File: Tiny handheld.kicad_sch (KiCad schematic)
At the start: 38 parts, among them J1 Conn_01x04_Female, J2 Conn_01x04_Female, J3 TYPE-C-31-M-12, U1 ATtiny85-20P, U2 ATtiny85-20M, U3 EEPROM-I2CEIAJ

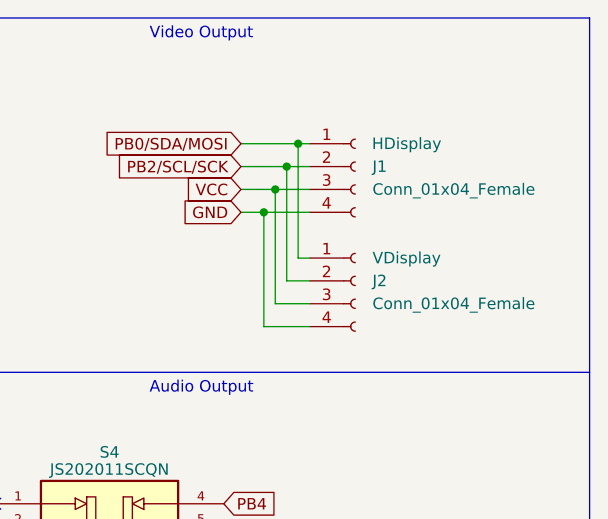
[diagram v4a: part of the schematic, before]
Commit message: removed vertical screen header
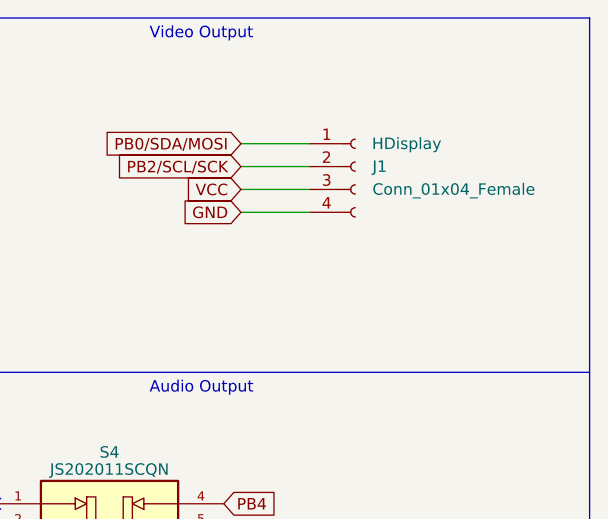
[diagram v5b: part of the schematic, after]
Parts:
- removed J2: Conn_01x04_Female, Connector_PinHeader_2.54mm:PinHeader_1x04_P2.54mm_Vertical, symbol Connector:Conn_01x04_Female
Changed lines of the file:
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@@
   (junction (at 132.715 57.15) (diameter 0) (color 0 0 0 0)
   )
-  (junction (at 245.745 34.925) (diameter 0) (color 0 0 0 0)
-  )
   (junction (at 130.175 29.845) (diameter 0) (color 0 0 0 0)
   )
@@
   (junction (at 54.61 100.33) (diameter 0) (color 0 0 0 0)
   )
-  (junction (at 249.555 27.305) (diameter 0) (color 0 0 0 0)
-  )
-  (junction (at 248.285 29.845) (diameter 0) (color 0 0 0 0)
-  )
   (junction (at 132.715 54.61) (diameter 0) (color 0 0 0 0)
   )
@@
   )
   (junction (at 36.83 34.925) (diameter 0) (color 0 0 0 0)
-  )
-  (junction (at 247.015 32.385) (diameter 0) (color 0 0 0 0)
   )
   (junction (at 130.175 32.385) (diameter 0) (color 0 0 0 0)
@@
     (stroke (width 0) (type default) (color 0 0 0 0))
   )
-  (wire (pts (xy 247.015 45.085) (xy 247.015 32.385))
-    (stroke (width 0) (type default) (color 0 0 0 0))
-  )
   (wire (pts (xy 123.825 107.315) (xy 128.905 107.315))
     (stroke (width 0) (type default) (color 0 0 0 0))
@@
     (stroke (width 0) (type default) (color 0 0 0 0))
   )
-  (wire (pts (xy 250.825 45.085) (xy 247.015 45.085))
-    (stroke (width 0) (type default) (color 0 0 0 0))
-  )
   (wire (pts (xy 35.56 70.485) (xy 39.37 70.485))
     (stroke (width 0) (type default) (color 0 0 0 0))
@@
     (stroke (width 0) (type default) (color 0 0 0 0))
   )
-  (wire (pts (xy 250.825 42.545) (xy 248.285 42.545))
-    (stroke (width 0) (type default) (color 0 0 0 0))
-  )
-  (wire (pts (xy 243.205 32.385) (xy 247.015 32.385))
-    (stroke (width 0) (type default) (color 0 0 0 0))
-  )
   (wire (pts (xy 53.34 57.785) (xy 53.34 61.595))
     (stroke (width 0) (type default) (color 0 0 0 0))
@@
     (stroke (width 0) (type default) (color 0 0 0 0))
   )
-  (wire (pts (xy 248.285 29.845) (xy 250.825 29.845))
+  (wire (pts (xy 243.205 29.845) (xy 250.825 29.845))
     (stroke (width 0) (type default) (color 0 0 0 0))
   )
@@
     (stroke (width 0) (type default) (color 0 0 0 0))
   )
-  (wire (pts (xy 245.745 34.925) (xy 250.825 34.925))
-    (stroke (width 0) (type default) (color 0 0 0 0))
-  )
-  (wire (pts (xy 250.825 47.625) (xy 245.745 47.625))
+  (wire (pts (xy 243.205 34.925) (xy 250.825 34.925))
     (stroke (width 0) (type default) (color 0 0 0 0))
   )
@@
     (stroke (width 0) (type default) (color 0 0 0 0))
   )
-  (wire (pts (xy 250.825 40.005) (xy 249.555 40.005))
-    (stroke (width 0) (type default) (color 0 0 0 0))
-  )
   (wire (pts (xy 53.34 83.185) (xy 53.34 85.725))
     (stroke (width 0) (type default) (color 0 0 0 0))
@@
     (stroke (width 0) (type default) (color 0 0 0 0))
   )
-  (wire (pts (xy 243.205 34.925) (xy 245.745 34.925))
-    (stroke (width 0) (type default) (color 0 0 0 0))
-  )
   (wire (pts (xy 167.005 32.385) (xy 173.355 32.385))
     (stroke (width 0) (type default) (color 0 0 0 0))
@@
     (stroke (width 0) (type default) (color 0 0 0 0))
   )
-  (wire (pts (xy 248.285 42.545) (xy 248.285 29.845))
-    (stroke (width 0) (type default) (color 0 0 0 0))
-  )
-  (wire (pts (xy 245.745 47.625) (xy 245.745 34.925))
-    (stroke (width 0) (type default) (color 0 0 0 0))
-  )
   (wire (pts (xy 42.545 111.76) (xy 42.545 114.3))
     (stroke (width 0) (type default) (color 0 0 0 0))
@@
     (stroke (width 0) (type default) (color 0 0 0 0))
   )
-  (wire (pts (xy 243.205 27.305) (xy 249.555 27.305))
+  (wire (pts (xy 243.205 27.305) (xy 250.825 27.305))
     (stroke (width 0) (type default) (color 0 0 0 0))
   )
@@
     (stroke (width 0) (type default) (color 0 0 0 0))
   )
-  (wire (pts (xy 249.555 40.005) (xy 249.555 27.305))
-    (stroke (width 0) (type default) (color 0 0 0 0))
-  )
-  (wire (pts (xy 247.015 32.385) (xy 250.825 32.385))
+  (wire (pts (xy 243.205 32.385) (xy 250.825 32.385))
     (stroke (width 0) (type default) (color 0 0 0 0))
   )
@@
     (stroke (width 0) (type default) (color 0 0 0 0))
   )
-  (wire (pts (xy 249.555 27.305) (xy 250.825 27.305))
-    (stroke (width 0) (type default) (color 0 0 0 0))
-  )
   (wire (pts (xy 42.545 116.84) (xy 42.545 119.38))
     (stroke (width 0) (type default) (color 0 0 0 0))
   )
   (wire (pts (xy 45.72 119.38) (xy 56.515 119.38))
-    (stroke (width 0) (type default) (color 0 0 0 0))
-  )
-  (wire (pts (xy 243.205 29.845) (xy 248.285 29.845))
     (stroke (width 0) (type default) (color 0 0 0 0))
   )
@@
     (pin "2")
   )
-  (symbol (lib_id "Connector:Conn_01x04_Female") (at 255.905 42.545 0) (unit 1)
-    (in_bom yes) (on_board yes)
-    (property "Reference" "J2" (id 0) (at 257.81 42.5449 0)
-      (effects (font (size 1.27 1.27)) (justify left))
-    )
-    (property "Value" "Conn_01x04_Female" (id 1) (at 257.81 45.0849 0)
-      (effects (font (size 1.27 1.27)) (justify left))
-    )
-    (property "Footprint" "Connector_PinHeader_2.54mm:PinHeader_1x04_P2.54mm_Vertical" (id 2) (at 255.905 42.545 0)
-      (effects (font (size 1.27 1.27)) hide)
-    )
-    (property "Datasheet" "~" (id 3) (at 255.905 42.545 0)
-      (effects (font (size 1.27 1.27)) hide)
-    )
-    (property "Purpose" "VDisplay" (id 4) (at 261.62 40.005 0))
-    (pin "1")
-    (pin "2")
-    (pin "3")
-    (pin "4")
-  )
   (symbol (lib_id "power:GND") (at 250.19 81.915 0) (unit 1)
     (in_bom yes) (on_board yes) (fields_autoplaced)
@@
       (reference "J1") (unit 1) (value "Conn_01x04_Female") (footprint "Connector_PinHeader_2.54mm:PinHeader_1x04_P2.54mm_Vertical")
     )
-    (path "/9e146ef5-55d1-47a4-b06d-46cb8cec31e9"
-      (reference "J2") (unit 1) (value "Conn_01x04_Female") (footprint "Connector_PinHeader_2.54mm:PinHeader_1x04_P2.54mm_Vertical")
-    )
     (path "/3f447363-eab1-44cf-bd61-e64a97ca5167"

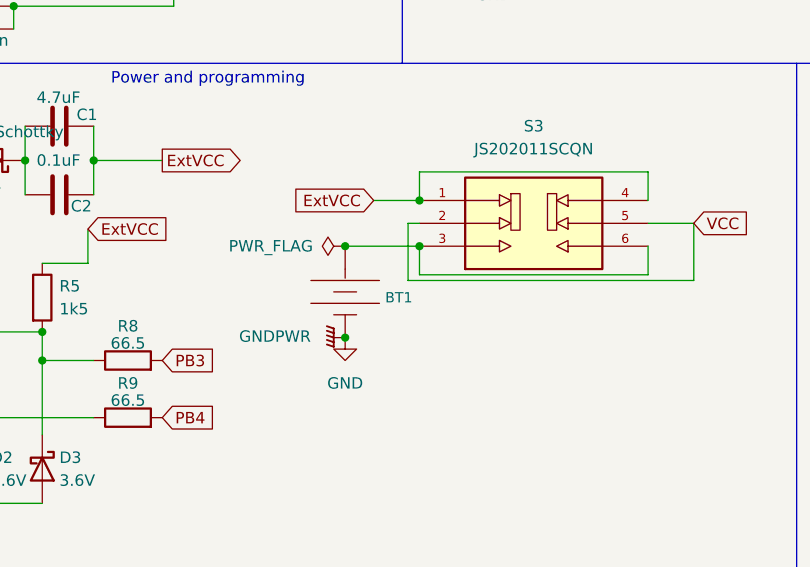
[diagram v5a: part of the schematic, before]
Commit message: first melted circuit tryout (rounded tracks)
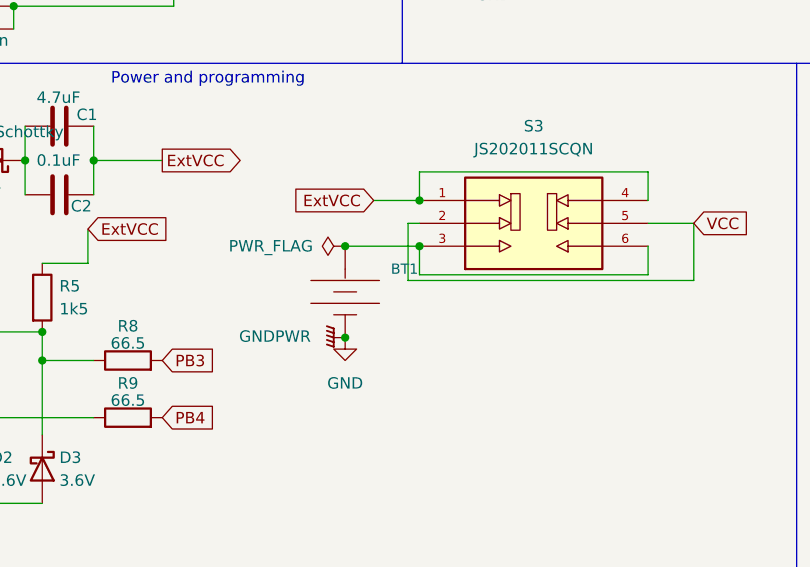
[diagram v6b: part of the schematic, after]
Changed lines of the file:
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@@
   (junction (at 132.715 57.15) (diameter 0) (color 0 0 0 0)
   )
+  (junction (at 90.17 120.015) (diameter 0) (color 0 0 0 0)
+  )
   (junction (at 130.175 29.845) (diameter 0) (color 0 0 0 0)
   )
@@
   (junction (at 48.895 128.905) (diameter 0) (color 0 0 0 0)
   )
+  (junction (at 90.17 109.855) (diameter 0) (color 0 0 0 0)
+  )
   (junction (at 54.61 100.33) (diameter 0) (color 0 0 0 0)
   )
@@
   (junction (at 116.84 76.835) (diameter 0) (color 0 0 0 0)
   )
-  (junction (at 90.17 109.855) (diameter 0) (color 0 0 0 0)
-  )
   (junction (at 48.895 138.43) (diameter 0) (color 0 0 0 0)
   )
@@
   )
   (junction (at 60.96 34.925) (diameter 0) (color 0 0 0 0)
-  )
-  (junction (at 90.17 120.015) (diameter 0) (color 0 0 0 0)
   )
   (junction (at 241.3 72.39) (diameter 0) (color 0 0 0 0)
@@
     (pin "2")
   )
-  (symbol (lib_id "SparkFun-Batteries:BATTERY-6.8MM_SMD") (at 90.17 114.935 270) (unit 1)
-    (in_bom yes) (on_board yes)
-    (property "Reference" "BT1" (id 0) (at 94.615 115.57 90)
-      (effects (font (size 1.143 1.143)) (justify left))
-    )
-    (property "Value" "BATTERY-6.8MM_SMD" (id 1) (at 94.615 114.935 90)
-      (effects (font (size 1.143 1.143)) (justify left) hide)
-    )
-    (property "Footprint" "Snapeda:BAT_BU2032-1" (id 2) (at 96.52 114.935 0)
-      (effects (font (size 0.508 0.508)) hide)
-    )
-    (property "Datasheet" "" (id 3) (at 90.17 114.935 0)
-      (effects (font (size 1.27 1.27)) hide)
-    )
-    (property "Field4" "BATT-13734" (id 4) (at 94.615 118.11 90)
-      (effects (font (size 1.524 1.524)) (justify left) hide)
-    )
-    (pin "+")
-    (pin "-")
-  )
   (symbol (lib_id "Jumper:SolderJumper_3_Bridged123") (at 160.655 64.77 180) (unit 1)
     (in_bom yes) (on_board yes) (fields_autoplaced)
@@
     (pin "1")
   )
+  (symbol (lib_id "SparkFun-Batteries:BATTERY-6.8MM_SMD") (at 90.17 114.935 270) (unit 1)
+    (in_bom yes) (on_board yes) (fields_autoplaced)
+    (property "Reference" "BT1" (id 0) (at 95.25 112.395 90)
+      (effects (font (size 1.143 1.143)) (justify left))
+    )
+    (property "Value" "BATTERY-6.8MM_SMD" (id 1) (at 95.25 114.935 90)
+      (effects (font (size 1.143 1.143)) (justify left) hide)
+    )
+    (property "Footprint" "Snapeda:BAT_BU2032-1" (id 2) (at 96.52 114.935 0)
+      (effects (font (size 0.508 0.508)) hide)
+    )
+    (property "Datasheet" "" (id 3) (at 90.17 114.935 0)
+      (effects (font (size 1.27 1.27)) hide)
+    )
+    (property "Field4" "BATT-13734" (id 4) (at 95.25 118.11 90)
+      (effects (font (size 1.524 1.524)) (justify left) hide)
+    )
+    (pin "+")
+    (pin "-")
+  )
   (symbol (lib_id "Jumper:SolderJumper_3_Bridged123") (at 53.34 45.085 90) (unit 1)
     (in_bom yes) (on_board yes) (fields_autoplaced)
@@
       (reference "#PWR0114") (unit 1) (value "GNDPWR") (footprint "")
     )
-    (path "/4b266b1c-a058-4abd-b8c0-7db2a93cb2d3"
+    (path "/d87d81d6-a9f7-455a-b1d8-8ff0988a0a64"
       (reference "BT1") (unit 1) (value "BATTERY-6.8MM_SMD") (footprint "Snapeda:BAT_BU2032-1")
     )

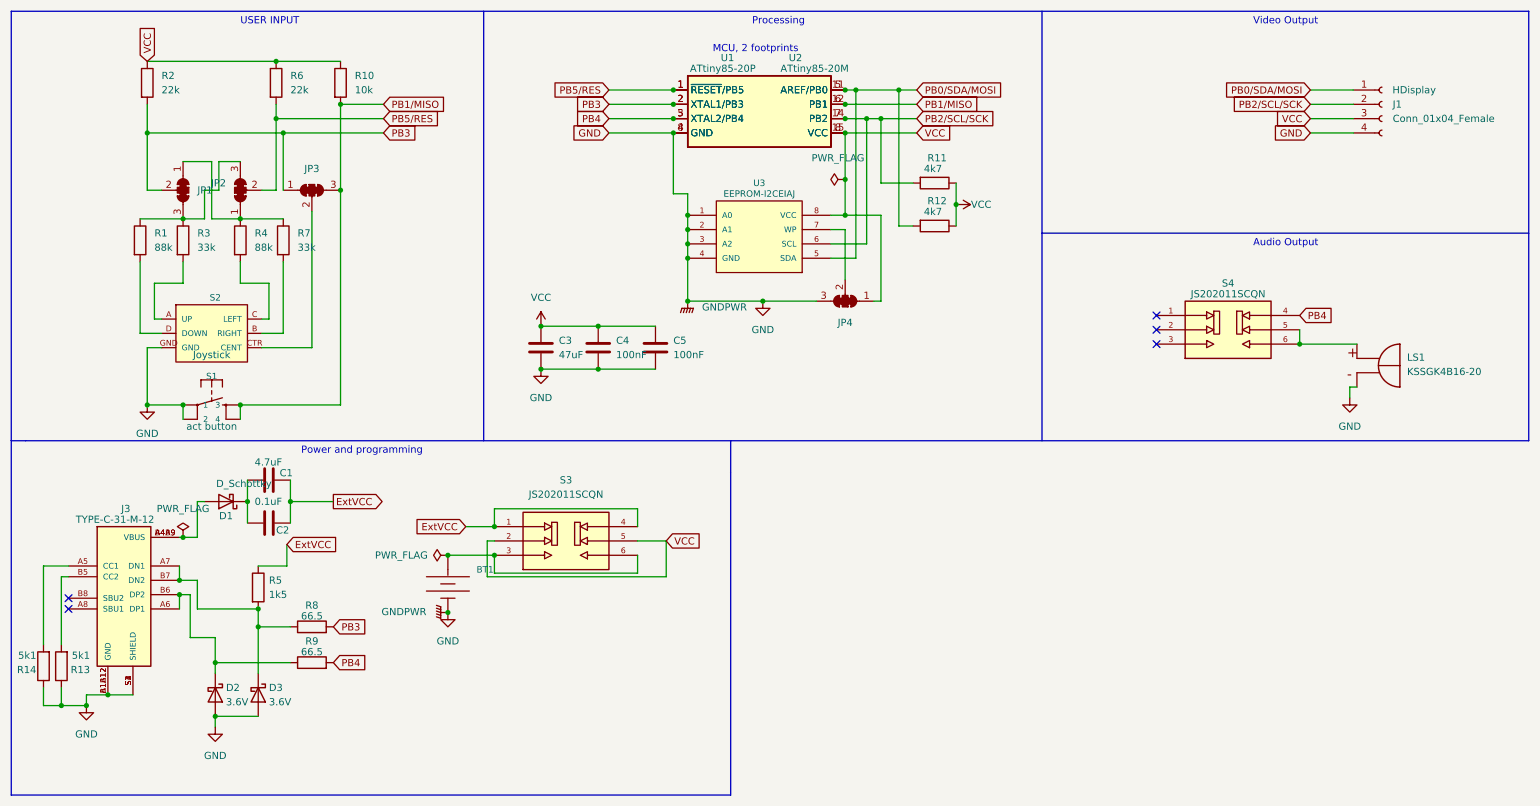
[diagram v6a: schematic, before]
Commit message: Start on V2.0
V1.0 could not be programmed easily via usb C, which was the whole point.
Going back to arduino ISP programmer.
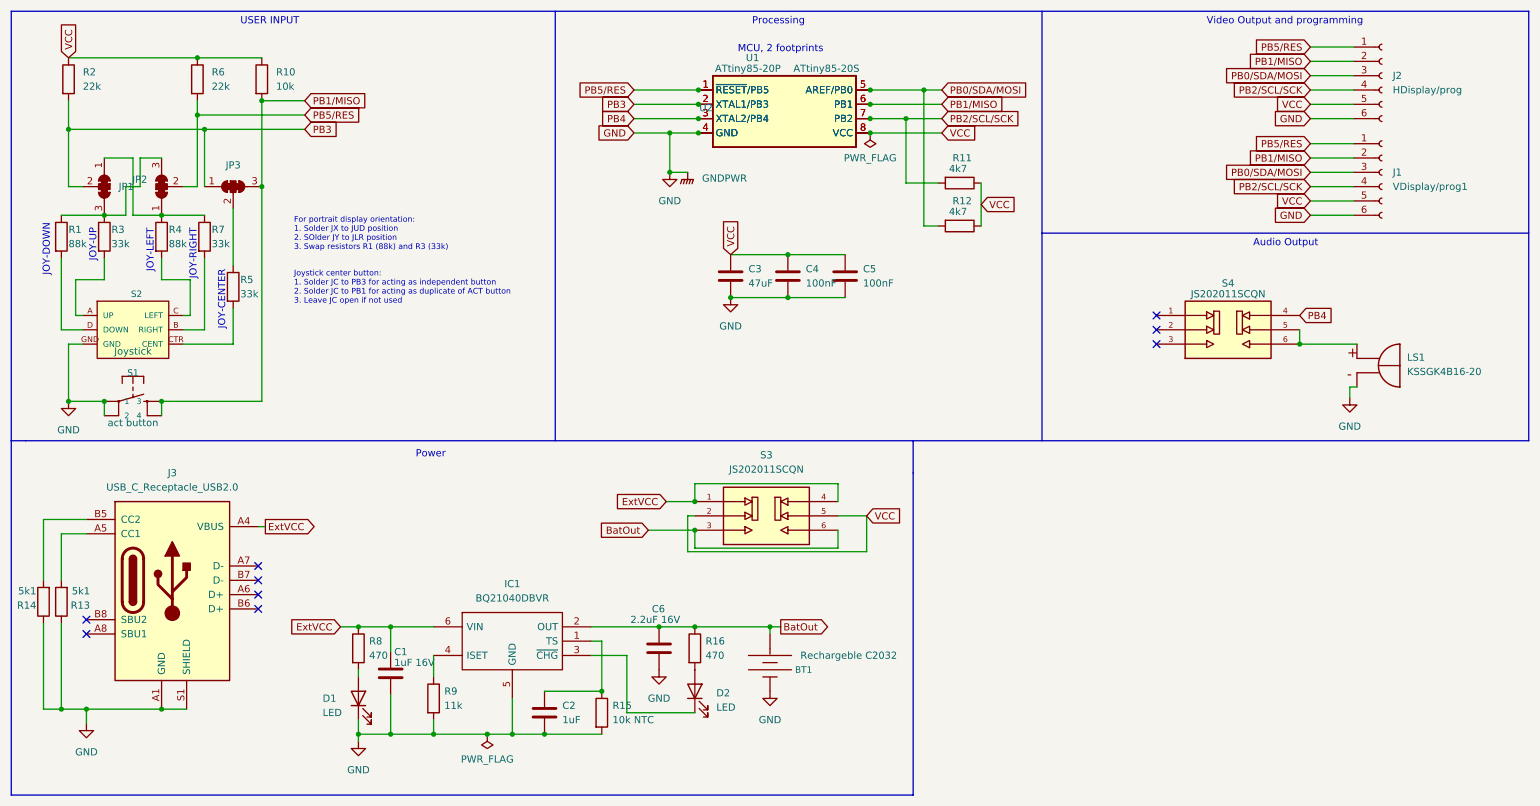
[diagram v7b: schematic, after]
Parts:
- removed D1: D_Schottky, Diode_SMD:D_1210_3225Metric_Pad1.42x2.65mm_HandSolder, symbol Device:D_Schottky
- removed D2, D3: 3.6V, Diode_SMD:D_1210_3225Metric_Pad1.42x2.65mm_HandSolder, symbol Device:D_Schottky
- removed J1: Conn_01x04_Female, Connector_PinHeader_2.54mm:PinHeader_1x04_P2.54mm_Vertical, symbol Connector:Conn_01x04_Female
- removed J3: TYPE-C-31-M-12, Snapeda:HRO_TYPE-C-31-M-12, symbol TYPE-C-31-M-12:TYPE-C-31-M-12
- removed JP4: SolderJumper_3_Bridged123, Jumper:SolderJumper-3_P1.3mm_Open_RoundedPad1.0x1.5mm_NumberLabels, symbol Jumper:SolderJumper_3_Bridged123
- removed U2: ATtiny85-20M, Snapeda:QFN50P400X400X80-21N, symbol MCU_Microchip_ATtiny:ATtiny85-20M
- removed U3: EEPROM-I2CEIAJ, Package_SO:SOIC-8_3.9x4.9mm_P1.27mm, symbol SparkFun-IC-Memory:EEPROM-I2CEIAJ
- added C6: 2.2uF 16V, Capacitor_SMD:C_1206_3216Metric_Pad1.33x1.80mm_HandSolder, symbol Device:C
- added D1, D2: LED, LED_SMD:LED_1206_3216Metric_Pad1.42x1.75mm_HandSolder, symbol Device:LED
- added IC1: BQ21040DBVR, Package_TO_SOT_SMD:SOT-23-6_Handsoldering, symbol SamacSys_Parts:BQ21040DBVR
- added J1: VDisplay/prog1, Connector_PinSocket_2.54mm:PinSocket_1x06_P2.54mm_Vertical, symbol Connector:Conn_01x06_Female
- added J2: HDisplay/prog, Connector_PinSocket_2.54mm:PinSocket_1x06_P2.54mm_Vertical, symbol Connector:Conn_01x06_Female
- added J3: USB_C_Receptacle_USB2.0, USB-C-Power-tester:TYPE-C-31-M-17_handsolder, symbol Connector:USB_C_Receptacle_USB2.0
- added R15: 10k NTC, Resistor_SMD:R_1206_3216Metric_Pad1.30x1.75mm_HandSolder, symbol Device:R
- added R16: 470, Resistor_SMD:R_1206_3216Metric_Pad1.30x1.75mm_HandSolder, symbol Device:R
- added U2: ATtiny85-20S, Package_SO:SOIC-8W_5.3x5.3mm_P1.27mm, symbol MCU_Microchip_ATtiny:ATtiny85-20S
- BT1: footprint Snapeda:BAT_BU2032-1 -> Battery:BatteryHolder_Keystone_3002_1x2032; Purpose (none) -> Rechargeble C2032
- C1: value 4.7uF -> 1uF 16V
- C2: value 0.1uF -> 1uF
- R5: value 1k5 -> 33k
- R8: value 66.5 -> 470
- R9: value 66.5 -> 11k
- U1: footprint Package_DIP:DIP-8_W7.62mm -> USB-C-Power-tester:TYPE-C-31-M-17
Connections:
- net ExtVCC: now also R8.1, IC1.6 (VIN), J3.A4 (VBUS), J3.A9 (VBUS), J3.B4 (VBUS), J3.B9 (VBUS); no longer C2.1, R5.1
- net GND: now also C1.2, C2.2, R9.2, C6.2, D1.1 (K), IC1.5 (GND), J1.6 (Pin_6), J2.6 (Pin_6), J3.A1 (GND), J3.A12 (GND), J3.B1 (GND), J3.B12 (GND), J3.S1 (SHIELD), R15.2, U2.4 (GND)
- net PB0/SDA/MOSI: now also J1.3 (Pin_3), J2.3 (Pin_3), U2.5 (AREF/PB0)
- net PB1/MISO: now also J1.2 (Pin_2), J2.2 (Pin_2), U2.6 (PB1)
- net PB2/SCL/SCK: now also J1.4 (Pin_4), J2.4 (Pin_4), U2.7 (PB2)
- net PB3: now also U2.2 (XTAL1/PB3); no longer R8.2
- net PB4: now also U2.3 (XTAL2/PB4); no longer R9.2
- net PB5/RES: now also J1.1 (Pin_1), J2.1 (Pin_1), U2.1 (~{RESET}/PB5)
- net VCC: now also J1.5 (Pin_5), J2.5 (Pin_5), U2.8 (VCC)
- net at R9.1: now also IC1.4 (ISET)
- net at JP3.2 (C): now also R5.1; no longer S2.CTR (CENT)
- net BatOut: now reaches BT1.+, S3.3, S3.6
- net BatOut: now also C6.1, IC1.2 (OUT), R16.1
- net at R5.2: now also S2.CTR (CENT); no longer R8.1
- net at R14.2: now also J3.B5 (CC2)
- net at R13.2: now also J3.A5 (CC1)
- new net: D2.2 (A), R16.2
- new net: D1.2 (A), R8.2
- new net: D2.1 (K), IC1.3 (~{CHG})
- new net: C2.1, IC1.1 (TS), R15.1
- no-connect marks 5 -> 9
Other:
- note added: "For portrait display orientation: 1. Solder JX to JUD position 2. SOlder JY to JLR position 3. Swap resistors R1 (88k) and R3 (33k)"
- note added: "JOY-CENTER"
- note added: "JOY-DOWN"
- note added: "JOY-LEFT"
- note added: "JOY-RIGHT"
- note added: "JOY-UP"
- note added: "Joystick center button: 1. Solder JC to PB3 for acting as independent button 2. Solder JC to PB1 for acting as duplicate of ACT button 3. Leave JC open if not used"
- note added: "Power"
- note added: "Video Output and programming"
- note removed: "Power and programming"
- note removed: "Video Output"
- moved on the sheet: BT1, C3, C4, C5, JP1, JP2, JP3, R1, R10, R11, R12, R13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

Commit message: New layout and silkscreen improvements
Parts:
- U1: footprint USB-C-Power-tester:TYPE-C-31-M-17 -> SamacSys_Parts:DIP781W56P254L950H533Q8N
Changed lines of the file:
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@@
       (effects (font (size 1.27 1.27)) (justify right))
     )
-    (property "Footprint" "USB-C-Power-tester:TYPE-C-31-M-17" (id 2) (at 151.765 61.595 0)
+    (property "Footprint" "SamacSys_Parts:DIP781W56P254L950H533Q8N" (id 2) (at 151.765 61.595 0)
       (effects (font (size 1.27 1.27) italic) hide)
     )
@@
     )
     (path "/716dbfd6-a7fb-46e6-a1fd-155b10b4ba36"
-      (reference "U1") (unit 1) (value "ATtiny85-20P") (footprint "USB-C-Power-tester:TYPE-C-31-M-17")
+      (reference "U1") (unit 1) (value "ATtiny85-20P") (footprint "SamacSys_Parts:DIP781W56P254L950H533Q8N")
     )
     (path "/ce77d059-5afe-4faf-9ead-57b1b83e54ae"
